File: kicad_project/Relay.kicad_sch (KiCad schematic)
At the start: 13 parts, among them J1 5018762640, J2 USB_C_Receptacle, J3 RJ45, K1 G6K-2P-Y_DC3, Q1 SO2222

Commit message: symbol SO2222 updated Symbol
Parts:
- removed Q1: SO2222, Package_TO_SOT_SMD:SOT-23, symbol Transistor_FET:AO3400A
- added Q1: SO2222, Package_TO_SOT_SMD:SOT-23, symbol Device:Q_NPN_BCE
- K1: value G6K-2P-Y_DC3 -> G6K-2P-Y_DC5
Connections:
- net GND: now also Q1.2 (C)
- net IGN: now also Q1.1 (B)
- net at R4.1: now also Q1.3 (E)
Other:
- moved on the sheet: CR1, R4

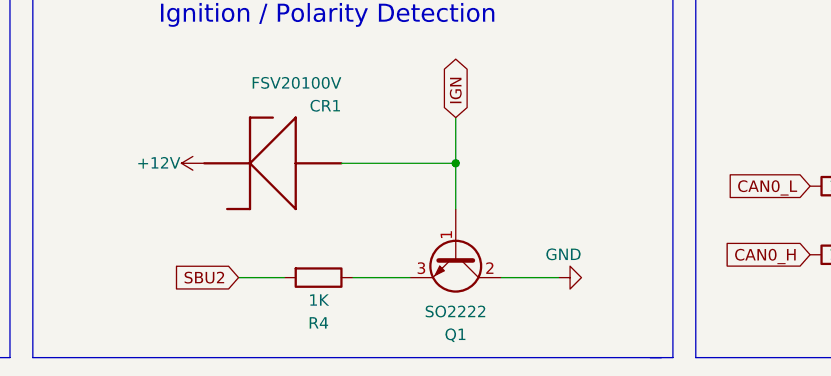
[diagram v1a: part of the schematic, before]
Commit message: new NPN Transistor
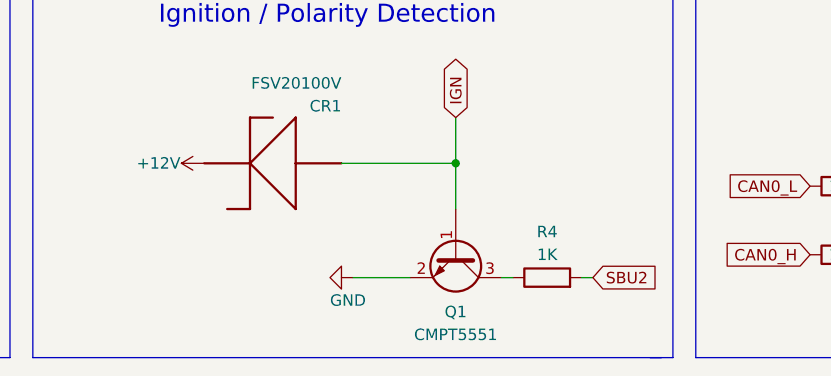
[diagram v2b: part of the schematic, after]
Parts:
- removed Q1: SO2222, Package_TO_SOT_SMD:SOT-23, symbol Device:Q_NPN_BCE
- added Q1: CMPT5551, Package_TO_SOT_SMD:SOT-23, symbol Transistor_BJT:BC817W
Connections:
- net GND: now also Q1.2 (E)
- net IGN: now also Q1.1 (B)
- net at R4.1: now also Q1.3 (C)
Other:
- moved on the sheet: R4
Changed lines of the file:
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@@
     (stroke (width 0) (type default) (color 0 0 0 0))
   )
-  (wire (pts (xy 146.05 149.86) (xy 140.97 149.86))
+  (wire (pts (xy 179.07 149.86) (xy 180.34 149.86))
     (stroke (width 0) (type default) (color 0 0 0 0))
   )
@@
     (stroke (width 0) (type default) (color 0 0 0 0))
   )
-  (wire (pts (xy 176.53 149.86) (xy 170.18 149.86))
+  (wire (pts (xy 153.67 149.86) (xy 160.02 149.86))
     (stroke (width 0) (type default) (color 0 0 0 0))
   )
@@
     (stroke (width 0) (type default) (color 0 0 0 0))
   )
-  (wire (pts (xy 160.02 149.86) (xy 153.67 149.86))
+  (wire (pts (xy 170.18 149.86) (xy 171.45 149.86))
     (stroke (width 0) (type default) (color 0 0 0 0))
   )
@@
     )
   )
-  (global_label "SBU2" (shape input) (at 140.97 149.86 180) (fields_autoplaced)
-    (effects (font (size 1.27 1.27)) (justify right))
-    (property "Intersheet References" "${INTERSHEET_REFS}" (id 0) (at 133.5374 149.7806 0)
-      (effects (font (size 1.27 1.27)) (justify right) hide)
+  (global_label "SBU2" (shape input) (at 180.34 149.86 0) (fields_autoplaced)
+    (effects (font (size 1.27 1.27)) (justify left))
+    (property "Intersheet References" "${INTERSHEET_REFS}" (id 0) (at 187.7726 149.9394 0)
+      (effects (font (size 1.27 1.27)) (justify left) hide)
     )
   )
@@
     )
   )
-  (symbol (lib_id "Device:Q_NPN_BCE") (at 165.1 147.32 270) (unit 1)
-    (in_bom yes) (on_board yes) (fields_autoplaced)
-    (property "Reference" "Q1" (id 0) (at 165.1 156.21 90))
-    (property "Value" "SO2222" (id 1) (at 165.1 153.67 90))
-    (property "Footprint" "Package_TO_SOT_SMD:SOT-23" (id 2) (at 167.64 152.4 0)
-      (effects (font (size 1.27 1.27)) hide)
-    )
-    (property "Datasheet" "~" (id 3) (at 165.1 147.32 0)
-      (effects (font (size 1.27 1.27)) hide)
-    )
-    (pin "1")
-    (pin "2")
-    (pin "3")
-  )
   (symbol (lib_id "BAV21W_RHG:BAV21W_RHG") (at 146.05 93.98 90) (unit 1)
     (in_bom yes) (on_board yes) (fields_autoplaced)
@@
     (property "PARTNO" "FSV20100VCT-ND" (id 4) (at 152.4 137.16 0)
       (effects (font (size 1.27 1.27)) (justify left bottom) hide)
+    )
+    (pin "1")
+    (pin "2")
+    (pin "3")
+  )
+  (symbol (lib_id "Transistor_BJT:BC817W") (at 165.1 147.32 270) (unit 1)
+    (in_bom yes) (on_board yes) (fields_autoplaced)
+    (property "Reference" "Q1" (id 0) (at 165.1 153.67 90))
+    (property "Value" "CMPT5551" (id 1) (at 165.1 156.21 90))
+    (property "Footprint" "Package_TO_SOT_SMD:SOT-23" (id 2) (at 163.195 152.4 0)
+      (effects (font (size 1.27 1.27) italic) (justify left) hide)
+    )
+    (property "Datasheet" "https://www.onsemi.com/pub/Collateral/BC818-D.pdf" (id 3) (at 165.1 147.32 0)
+      (effects (font (size 1.27 1.27)) (justify left) hide)
     )
     (pin "1")
@@
     (pin "1")
   )
-  (symbol (lib_id "Device:R") (at 149.86 149.86 270) (unit 1)
-    (in_bom yes) (on_board yes)
-    (property "Reference" "R4" (id 0) (at 149.86 154.94 90))
-    (property "Value" "1K" (id 1) (at 149.86 152.4 90))
-    (property "Footprint" "Resistor_SMD:R_2010_5025Metric_Pad1.40x2.65mm_HandSolder" (id 2) (at 149.86 148.082 90)
-      (effects (font (size 1.27 1.27)) hide)
-    )
-    (property "Datasheet" "~" (id 3) (at 149.86 149.86 0)
+  (symbol (lib_id "Device:R") (at 175.26 149.86 90) (unit 1)
+    (in_bom yes) (on_board yes)
+    (property "Reference" "R4" (id 0) (at 175.26 144.78 90))
+    (property "Value" "1K" (id 1) (at 175.26 147.32 90))
+    (property "Footprint" "Resistor_SMD:R_2010_5025Metric_Pad1.40x2.65mm_HandSolder" (id 2) (at 175.26 151.638 90)
+      (effects (font (size 1.27 1.27)) hide)
+    )
+    (property "Datasheet" "~" (id 3) (at 175.26 149.86 0)
       (effects (font (size 1.27 1.27)) hide)
     )
@@
     (pin "9")
   )
-  (symbol (lib_id "power:GND") (at 176.53 149.86 90) (unit 1)
-    (in_bom yes) (on_board yes)
-    (property "Reference" "#PWR0103" (id 0) (at 182.88 149.86 0)
-      (effects (font (size 1.27 1.27)) hide)
-    )
-    (property "Value" "GND" (id 1) (at 179.07 147.32 90)
+  (symbol (lib_id "power:GND") (at 153.67 149.86 270) (unit 1)
+    (in_bom yes) (on_board yes)
+    (property "Reference" "#PWR0103" (id 0) (at 147.32 149.86 0)
+      (effects (font (size 1.27 1.27)) hide)
+    )
+    (property "Value" "GND" (id 1) (at 151.13 152.4 90)
       (effects (font (size 1.27 1.27)) (justify left))
     )
-    (property "Footprint" "" (id 2) (at 176.53 149.86 0)
-      (effects (font (size 1.27 1.27)) hide)
-    )
-    (property "Datasheet" "" (id 3) (at 176.53 149.86 0)
+    (property "Footprint" "" (id 2) (at 153.67 149.86 0)
+      (effects (font (size 1.27 1.27)) hide)
+    )
+    (property "Datasheet" "" (id 3) (at 153.67 149.86 0)
       (effects (font (size 1.27 1.27)) hide)
     )
@@
       (reference "K1") (unit 1) (value "G6K-2P-Y_DC5") (footprint "Relay:RELAY_G6K-2P-Y_DC3")
     )
-    (path "/00c322f6-2f4a-417b-a9f3-e5aa21e140af"
-      (reference "Q1") (unit 1) (value "SO2222") (footprint "Package_TO_SOT_SMD:SOT-23")
+    (path "/3b96dd1f-6d50-42aa-a2cb-6b3371b0fc1e"
+      (reference "Q1") (unit 1) (value "CMPT5551") (footprint "Package_TO_SOT_SMD:SOT-23")
     )
     (path "/aecf3d86-5150-491a-a65a-7fc5532943ba"

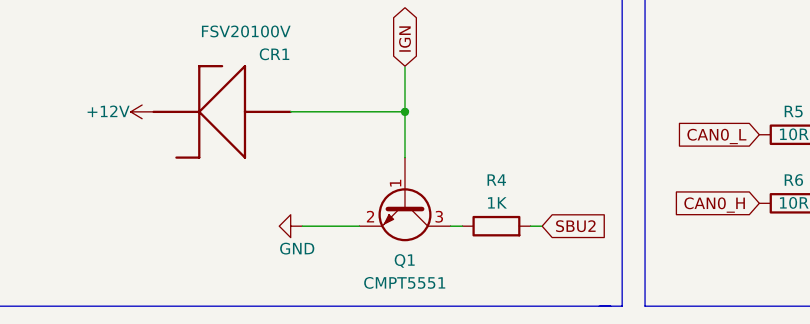
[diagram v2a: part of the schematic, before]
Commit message: back to SO2222 NPN Transistor
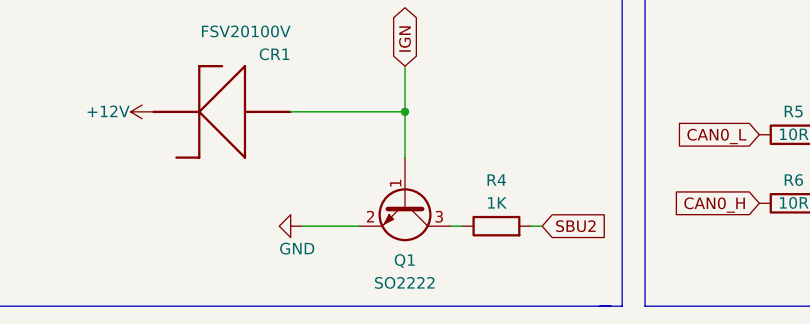
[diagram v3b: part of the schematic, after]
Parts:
- Q1: value CMPT5551 -> SO2222
- R5, R6: footprint Resistor_SMD:R_2010_5025Metric_Pad1.40x2.65mm_HandSolder -> Resistor_SMD:R_0603_1608Metric
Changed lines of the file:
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@@
     (property "Reference" "R6" (id 0) (at 208.28 144.78 90))
     (property "Value" "10R" (id 1) (at 208.28 147.32 90))
-    (property "Footprint" "Resistor_SMD:R_2010_5025Metric_Pad1.40x2.65mm_HandSolder" (id 2) (at 208.28 149.098 90)
+    (property "Footprint" "Resistor_SMD:R_0603_1608Metric" (id 2) (at 208.28 149.098 90)
       (effects (font (size 1.27 1.27)) hide)
     )
@@
     (in_bom yes) (on_board yes) (fields_autoplaced)
     (property "Reference" "Q1" (id 0) (at 165.1 153.67 90))
-    (property "Value" "CMPT5551" (id 1) (at 165.1 156.21 90))
+    (property "Value" "SO2222" (id 1) (at 165.1 156.21 90))
     (property "Footprint" "Package_TO_SOT_SMD:SOT-23" (id 2) (at 163.195 152.4 0)
       (effects (font (size 1.27 1.27) italic) (justify left) hide)
@@
     (property "Reference" "R5" (id 0) (at 208.28 137.16 90))
     (property "Value" "10R" (id 1) (at 208.28 139.7 90))
-    (property "Footprint" "Resistor_SMD:R_2010_5025Metric_Pad1.40x2.65mm_HandSolder" (id 2) (at 208.28 141.478 90)
+    (property "Footprint" "Resistor_SMD:R_0603_1608Metric" (id 2) (at 208.28 141.478 90)
       (effects (font (size 1.27 1.27)) hide)
     )
@@
     )
     (path "/3b96dd1f-6d50-42aa-a2cb-6b3371b0fc1e"
-      (reference "Q1") (unit 1) (value "CMPT5551") (footprint "Package_TO_SOT_SMD:SOT-23")
+      (reference "Q1") (unit 1) (value "SO2222") (footprint "Package_TO_SOT_SMD:SOT-23")
     )
     (path "/aecf3d86-5150-491a-a65a-7fc5532943ba"
@@
     )
     (path "/9082a5b8-b931-4a90-9fc7-b83f10b93a4b"
-      (reference "R5") (unit 1) (value "10R") (footprint "Resistor_SMD:R_2010_5025Metric_Pad1.40x2.65mm_HandSolder")
+      (reference "R5") (unit 1) (value "10R") (footprint "Resistor_SMD:R_0603_1608Metric")
     )
     (path "/2ebd1ab7-6b00-4f47-9ae5-5b1a5cb895f3"
-      (reference "R6") (unit 1) (value "10R") (footprint "Resistor_SMD:R_2010_5025Metric_Pad1.40x2.65mm_HandSolder")
+      (reference "R6") (unit 1) (value "10R") (footprint "Resistor_SMD:R_0603_1608Metric")
     )
     (path "/61ca9abc-6f18-4305-a8c6-737a044688c3"

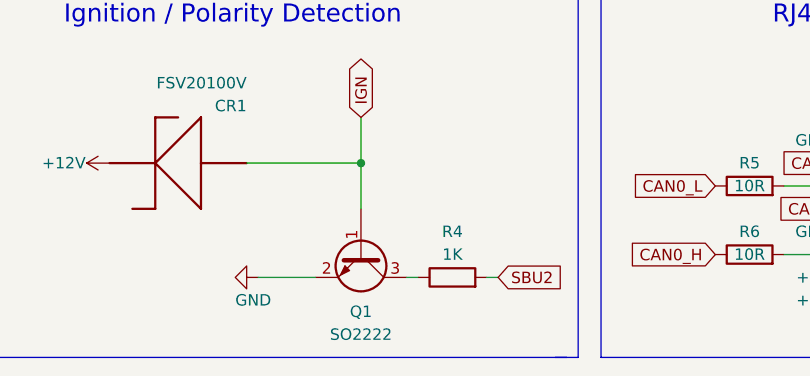
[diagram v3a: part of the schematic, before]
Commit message: finally fixed Transistor Issue. credits to mlocoteta
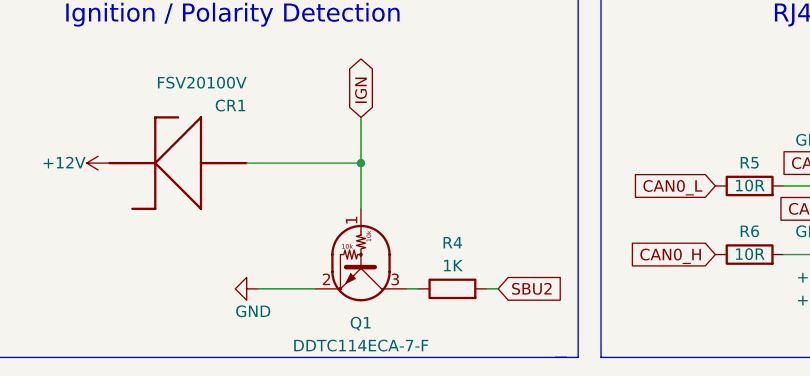
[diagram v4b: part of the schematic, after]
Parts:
- removed Q1: SO2222, Package_TO_SOT_SMD:SOT-23, symbol Transistor_BJT:BC817W
- added Q1: DDTC114ECA-7-F, Package_TO_SOT_SMD:SOT-23, symbol Transistor_BJT:DTC114E
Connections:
- net GND: now also Q1.2 (E)
- net IGN: now also Q1.1 (B)
- net at R4.1: now also Q1.3 (C)
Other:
- moved on the sheet: R4
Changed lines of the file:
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@@
     (stroke (width 0) (type default) (color 0 0 0 0))
   )
-  (wire (pts (xy 179.07 149.86) (xy 180.34 149.86))
+  (wire (pts (xy 179.07 151.13) (xy 180.34 151.13))
     (stroke (width 0) (type default) (color 0 0 0 0))
   )
@@
     (stroke (width 0) (type default) (color 0 0 0 0))
   )
-  (wire (pts (xy 153.67 149.86) (xy 160.02 149.86))
+  (wire (pts (xy 153.67 151.13) (xy 160.02 151.13))
     (stroke (width 0) (type default) (color 0 0 0 0))
   )
@@
     (stroke (width 0) (type default) (color 0 0 0 0))
   )
-  (wire (pts (xy 170.18 149.86) (xy 171.45 149.86))
+  (wire (pts (xy 170.18 151.13) (xy 171.45 151.13))
     (stroke (width 0) (type default) (color 0 0 0 0))
   )
@@
     )
   )
-  (global_label "SBU2" (shape input) (at 180.34 149.86 0) (fields_autoplaced)
+  (global_label "SBU2" (shape input) (at 180.34 151.13 0) (fields_autoplaced)
     (effects (font (size 1.27 1.27)) (justify left))
-    (property "Intersheet References" "${INTERSHEET_REFS}" (id 0) (at 187.7726 149.9394 0)
+    (property "Intersheet References" "${INTERSHEET_REFS}" (id 0) (at 187.7726 151.2094 0)
       (effects (font (size 1.27 1.27)) (justify left) hide)
     )
@@
     (property "PARTNO" "FSV20100VCT-ND" (id 4) (at 152.4 137.16 0)
       (effects (font (size 1.27 1.27)) (justify left bottom) hide)
-    )
-    (pin "1")
-    (pin "2")
-    (pin "3")
-  )
-  (symbol (lib_id "Transistor_BJT:BC817W") (at 165.1 147.32 270) (unit 1)
-    (in_bom yes) (on_board yes) (fields_autoplaced)
-    (property "Reference" "Q1" (id 0) (at 165.1 153.67 90))
-    (property "Value" "SO2222" (id 1) (at 165.1 156.21 90))
-    (property "Footprint" "Package_TO_SOT_SMD:SOT-23" (id 2) (at 163.195 152.4 0)
-      (effects (font (size 1.27 1.27) italic) (justify left) hide)
-    )
-    (property "Datasheet" "https://www.onsemi.com/pub/Collateral/BC818-D.pdf" (id 3) (at 165.1 147.32 0)
-      (effects (font (size 1.27 1.27)) (justify left) hide)
     )
     (pin "1")
@@
     (pin "1")
   )
-  (symbol (lib_id "Device:R") (at 175.26 149.86 90) (unit 1)
-    (in_bom yes) (on_board yes)
-    (property "Reference" "R4" (id 0) (at 175.26 144.78 90))
-    (property "Value" "1K" (id 1) (at 175.26 147.32 90))
-    (property "Footprint" "Resistor_SMD:R_2010_5025Metric_Pad1.40x2.65mm_HandSolder" (id 2) (at 175.26 151.638 90)
-      (effects (font (size 1.27 1.27)) hide)
-    )
-    (property "Datasheet" "~" (id 3) (at 175.26 149.86 0)
+  (symbol (lib_id "Device:R") (at 175.26 151.13 90) (unit 1)
+    (in_bom yes) (on_board yes)
+    (property "Reference" "R4" (id 0) (at 175.26 146.05 90))
+    (property "Value" "1K" (id 1) (at 175.26 148.59 90))
+    (property "Footprint" "Resistor_SMD:R_2010_5025Metric_Pad1.40x2.65mm_HandSolder" (id 2) (at 175.26 152.908 90)
+      (effects (font (size 1.27 1.27)) hide)
+    )
+    (property "Datasheet" "~" (id 3) (at 175.26 151.13 0)
       (effects (font (size 1.27 1.27)) hide)
     )
@@
     )
     (pin "1")
+  )
+  (symbol (lib_id "Transistor_BJT:DTC114E") (at 165.1 148.59 270) (unit 1)
+    (in_bom yes) (on_board yes) (fields_autoplaced)
+    (property "Reference" "Q1" (id 0) (at 165.1 154.94 90))
+    (property "Value" "DDTC114ECA-7-F " (id 1) (at 165.1 157.48 90))
+    (property "Footprint" "Package_TO_SOT_SMD:SOT-23" (id 2) (at 165.1 148.59 0)
+      (effects (font (size 1.27 1.27)) (justify left) hide)
+    )
+    (property "Datasheet" "" (id 3) (at 165.1 148.59 0)
+      (effects (font (size 1.27 1.27)) (justify left) hide)
+    )
+    (pin "1")
+    (pin "2")
+    (pin "3")
   )
   (symbol (lib_id "power:+12V") (at 220.98 149.86 90) (unit 1)
@@
     (pin "9")
   )
-  (symbol (lib_id "power:GND") (at 153.67 149.86 270) (unit 1)
-    (in_bom yes) (on_board yes)
-    (property "Reference" "#PWR0103" (id 0) (at 147.32 149.86 0)
-      (effects (font (size 1.27 1.27)) hide)
-    )
-    (property "Value" "GND" (id 1) (at 151.13 152.4 90)
+  (symbol (lib_id "power:GND") (at 153.67 151.13 270) (unit 1)
+    (in_bom yes) (on_board yes)
+    (property "Reference" "#PWR0103" (id 0) (at 147.32 151.13 0)
+      (effects (font (size 1.27 1.27)) hide)
+    )
+    (property "Value" "GND" (id 1) (at 151.13 153.67 90)
       (effects (font (size 1.27 1.27)) (justify left))
     )
-    (property "Footprint" "" (id 2) (at 153.67 149.86 0)
-      (effects (font (size 1.27 1.27)) hide)
-    )
-    (property "Datasheet" "" (id 3) (at 153.67 149.86 0)
+    (property "Footprint" "" (id 2) (at 153.67 151.13 0)
+      (effects (font (size 1.27 1.27)) hide)
+    )
+    (property "Datasheet" "" (id 3) (at 153.67 151.13 0)
       (effects (font (size 1.27 1.27)) hide)
     )
@@
       (reference "K1") (unit 1) (value "G6K-2P-Y_DC5") (footprint "Relay:RELAY_G6K-2P-Y_DC3")
     )
-    (path "/3b96dd1f-6d50-42aa-a2cb-6b3371b0fc1e"
-      (reference "Q1") (unit 1) (value "SO2222") (footprint "Package_TO_SOT_SMD:SOT-23")
+    (path "/bb9a8a2e-1b84-4351-b3b2-ef5c177e7a7d"
+      (reference "Q1") (unit 1) (value "DDTC114ECA-7-F ") (footprint "Package_TO_SOT_SMD:SOT-23")
     )
     (path "/aecf3d86-5150-491a-a65a-7fc5532943ba"
